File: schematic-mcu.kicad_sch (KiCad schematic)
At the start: 25 parts, among them U5 USBLC6-2P6, U6 ESP32-S3FN8, Y1 Crystal_GND24

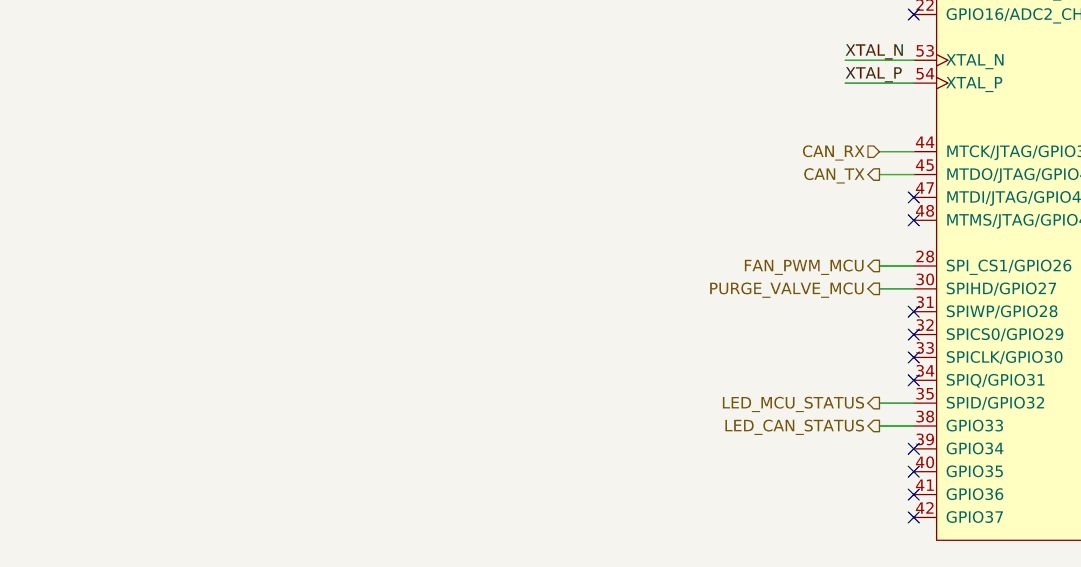
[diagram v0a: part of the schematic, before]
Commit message: Add power stages
Valve, power supplay, fan
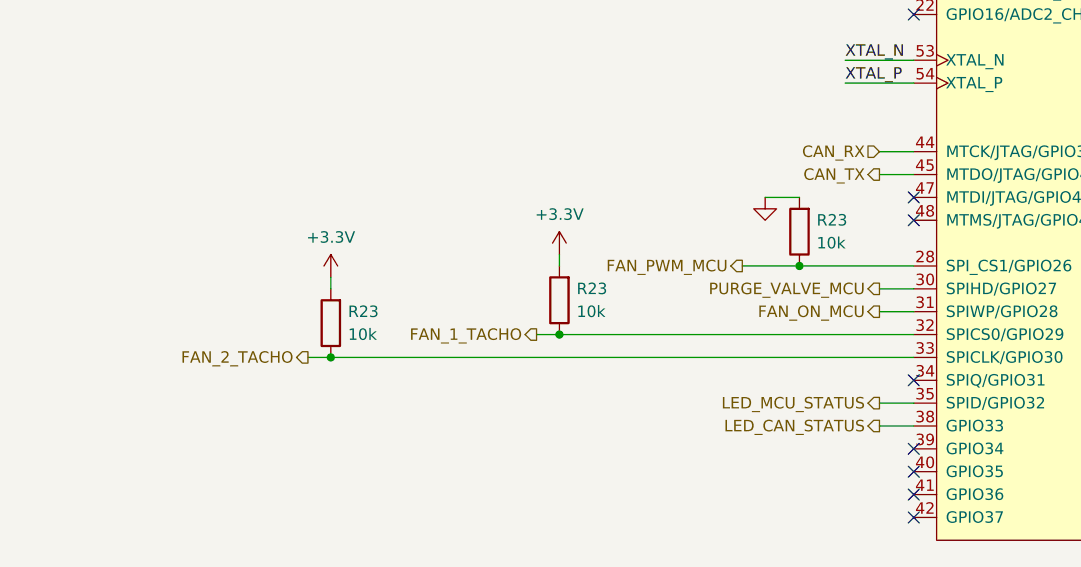
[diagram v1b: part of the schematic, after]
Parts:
- added R23 (x3): 10k, symbol Device:R
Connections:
- net +3.3V: now also R23.2, R23.2
- net FAN_PWM_MCU: now also R23.1
- net GND: now also R23.2
- net FAN_ON_MCU: now reaches U6.31 (SPIWP/GPIO28)
- net FAN_1_TACHO: now reaches U6.32 (SPICS0/GPIO29)
- net FAN_1_TACHO: now also R23.1
- net FAN_2_TACHO: now reaches U6.33 (SPICLK/GPIO30)
- net FAN_2_TACHO: now also R23.1
- no-connect marks 37 -> 34

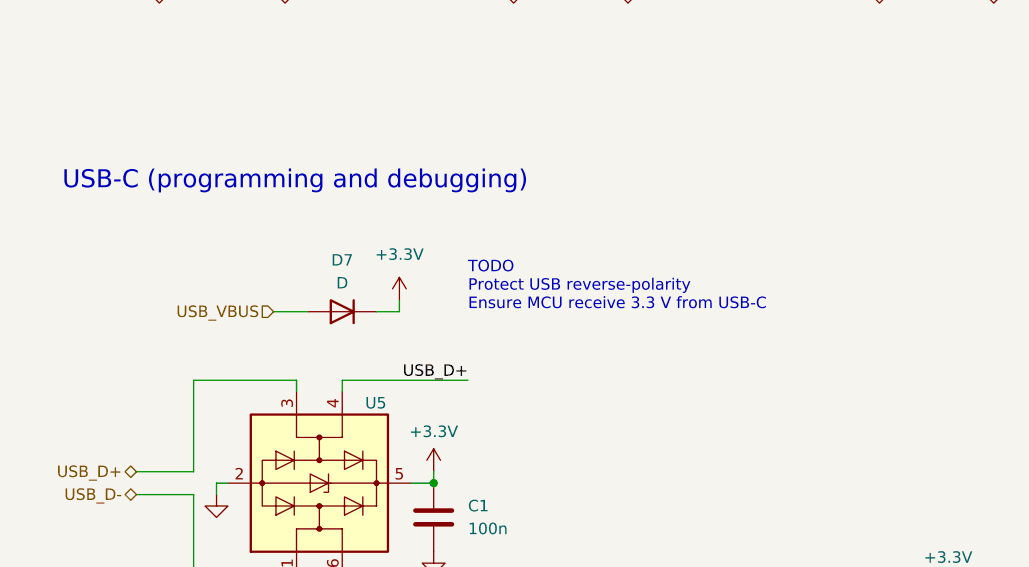
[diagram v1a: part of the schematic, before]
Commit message: Add Schottky Diode for VBUS and Vreg
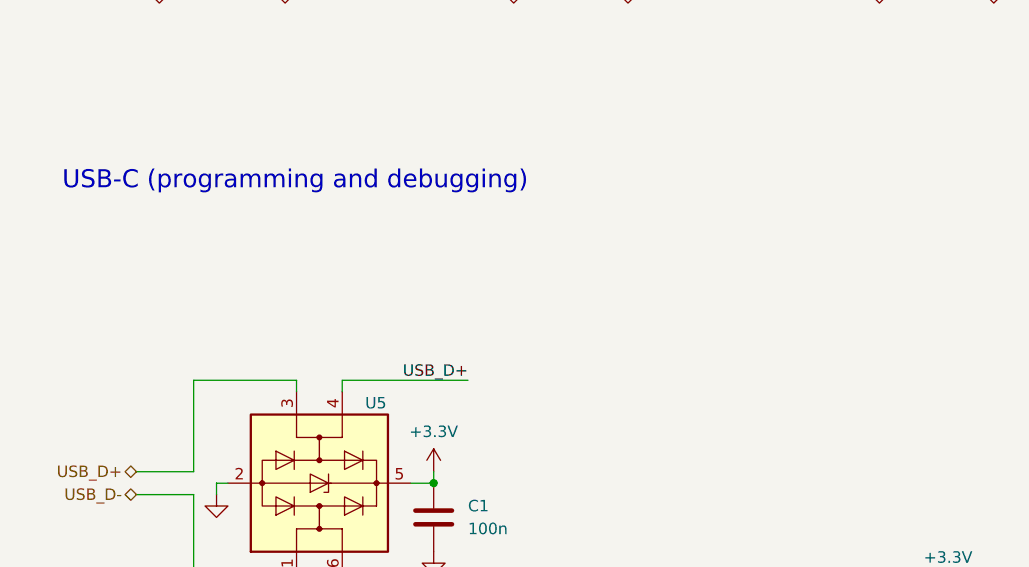
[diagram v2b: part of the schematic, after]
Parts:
- removed D7: D, symbol Device:D
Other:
- note removed: "TODO Protect USB reverse-polarity Ensure MCU receive 3.3 V from USB-C"
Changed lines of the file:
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@@
-    (stroke (width 0) (type default))
-  )
-  (wire (pts (xy 69.85 87.63) (xy 69.85 86.36))
     (stroke (width 0) (type default))
   )
@@
     (stroke (width 0) (type default))
   )
-  (wire (pts (xy 55.88 87.63) (xy 59.69 87.63))
-    (stroke (width 0) (type default))
-  )
   (wire (pts (xy 191.77 135.89) (xy 195.58 135.89))
     (stroke (width 0) (type default))
@@
   )
   (wire (pts (xy 270.51 85.09) (xy 261.62 85.09))
-    (stroke (width 0) (type default))
-  )
-  (wire (pts (xy 67.31 87.63) (xy 69.85 87.63))
     (stroke (width 0) (type default))
   )
@@
   (text "Microcontroller" (at 214.63 22.86 0)
     (effects (font (size 2 2)) (justify left bottom))
-  )
-  (text "TODO\nProtect USB reverse-polarity\nEnsure MCU receive 3.3 V from USB-C\n"
-    (at 77.47 87.63 0)
-    (effects (font (size 1.27 1.27)) (justify left bottom))
   )
   (text "Reset button" (at 49.53 25.4 0)
@@
   )
   (hierarchical_label "FAN_PWM_MCU" (shape output) (at 176.53 118.11 180) (fields_autoplaced)
-    (effects (font (size 1.27 1.27)) (justify right))
-  )
-  (hierarchical_label "USB_VBUS" (shape input) (at 55.88 87.63 180) (fields_autoplaced)
     (effects (font (size 1.27 1.27)) (justify right))
   )
@@
     )
   )
-  (symbol (lib_id "power:+3.3V") (at 69.85 86.36 0) (unit 1)
-    (in_bom yes) (on_board yes) (dnp no) (fields_autoplaced)
-    (property "Reference" "#PWR036" (at 69.85 90.17 0)
-      (effects (font (size 1.27 1.27)) hide)
-    )
-    (property "Value" "+3.3V" (at 69.85 81.28 0)
-      (effects (font (size 1.27 1.27)))
-    )
-    (property "Footprint" "" (at 69.85 86.36 0)
-      (effects (font (size 1.27 1.27)) hide)
-    )
-    (property "Datasheet" "" (at 69.85 86.36 0)
-      (effects (font (size 1.27 1.27)) hide)
-    )
-    (pin "1")
-    (instances
-      (project "schematic-main"
-        (path "/c9ad7189-d3b2-414a-9743-efd8e57cd755"
-          (reference "#PWR036") (unit 1)
-        )
-        (path "/c9ad7189-d3b2-414a-9743-efd8e57cd755/f92f58ec-64e0-437c-bc00-8ae46a3b3054"
-          (reference "#PWR028") (unit 1)
-        )
-      )
-    )
-  )
   (symbol (lib_id "power:GND") (at 73.66 114.3 0) (unit 1)
     (in_bom yes) (on_board yes) (dnp no) (fields_autoplaced)
@@
         )
       )
-    )
-  )
-  (symbol (lib_id "Device:D") (at 63.5 87.63 180) (unit 1)
-    (in_bom yes) (on_board yes) (dnp no) (fields_autoplaced)
-    (property "Reference" "D7" (at 63.5 81.915 0)
-      (effects (font (size 1.27 1.27)))
-    )
-    (property "Value" "D" (at 63.5 84.455 0)
-      (effects (font (size 1.27 1.27)))
-    )
-    (property "Footprint" "" (at 63.5 87.63 0)
-      (effects (font (size 1.27 1.27)) hide)
-    )
-    (property "Datasheet" "~" (at 63.5 87.63 0)
-      (effects (font (size 1.27 1.27)) hide)
-    )
-    (property "Sim.Device" "D" (at 63.5 87.63 0)
-      (effects (font (size 1.27 1.27)) hide)
-    )
-    (property "Sim.Pins" "1=K 2=A" (at 63.5 87.63 0)
-      (effects (font (size 1.27 1.27)) hide)
-    )
-    (pin "1")
-    (pin "2")
-    (instances
-      (project "schematic-main"
-        (path "/c9ad7189-d3b2-414a-9743-efd8e57cd755"
-          (reference "D7") (unit 1)
-        )
-        (path "/c9ad7189-d3b2-414a-9743-efd8e57cd755/f92f58ec-64e0-437c-bc00-8ae46a3b3054"
-          (reference "D2") (unit 1)
-        )
-      )

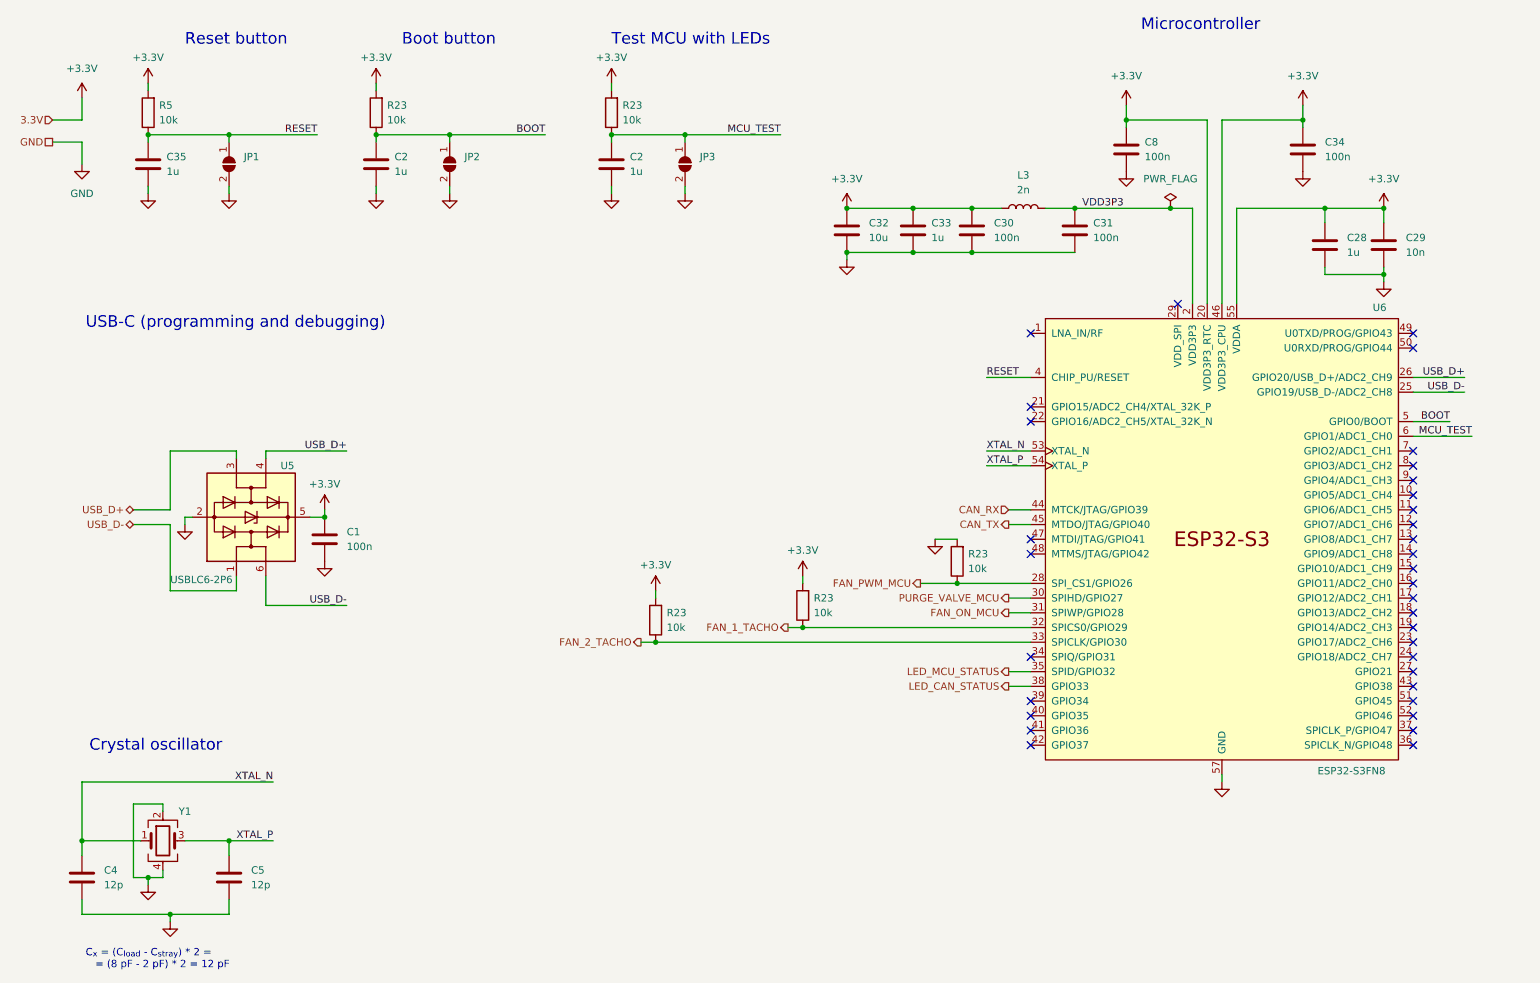
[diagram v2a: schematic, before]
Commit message: Add FC voltage measure, axilary input and output
Schematic complet?
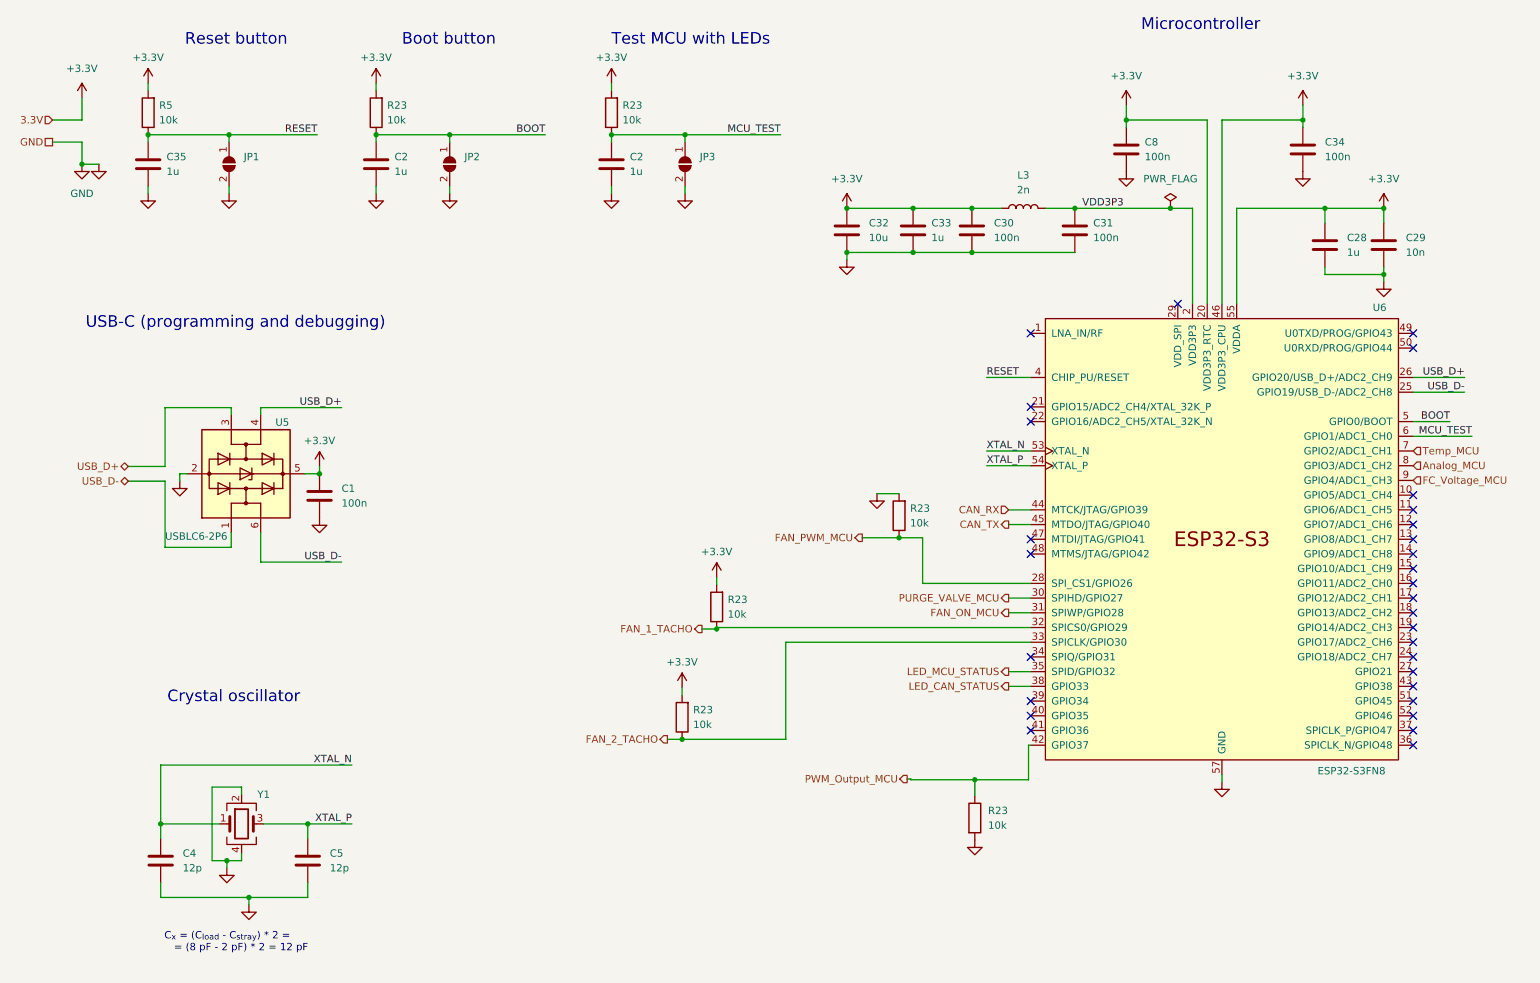
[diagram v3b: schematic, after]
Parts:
- added R23: 10k, symbol Device:R
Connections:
- net GND: now also R23.2
- net PWM_Output_MCU: now reaches U6.42 (GPIO37)
- net PWM_Output_MCU: now also R23.1
- net Temp_MCU: now reaches U6.7 (GPIO2/ADC1_CH1)
- net Analog_MCU: now reaches U6.8 (GPIO3/ADC1_CH2)
- net FC_Voltage_MCU: now reaches U6.9 (GPIO4/ADC1_CH3)
- no-connect marks 34 -> 30
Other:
- title: Motor driver unit -> Fuel Cell Control Unit  (FCCU)
- moved on the sheet: C1, C4, C5, R23, U5, Y1

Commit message: First pcb, change fan conector
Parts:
- C1, C2, C28, C29, C30, C31, C33, C34, C35, C4, C5, C8: footprint (none) -> Capacitor_SMD:C_1206_3216Metric
- C32: footprint (none) -> Capacitor_SMD:CP_Elec_8x10.5
- L3: footprint (none) -> Inductor_SMD:LQG15WH0N7B02D
- R23: footprint (none) -> LED_SMD:LED_1206_3216Metric
- R23, R5: footprint (none) -> Resistor_SMD:R_1206_3216Metric
- Y1: footprint (none) -> Crystal:KC3225K400000C1GE00
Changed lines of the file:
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@@
       (effects (font (size 1.27 1.27)) (justify left))
     )
-    (property "Footprint" "" (at 186.3852 60.96 0)
+    (property "Footprint" "Capacitor_SMD:C_1206_3216Metric" (at 186.3852 60.96 0)
       (effects (font (size 1.27 1.27)) hide)
     )
@@
       (effects (font (size 1.27 1.27)) (justify left))
     )
-    (property "Footprint" "" (at 164.7952 60.96 0)
+    (property "Footprint" "Capacitor_SMD:CP_Elec_8x10.5" (at 164.7952 60.96 0)
       (effects (font (size 1.27 1.27)) hide)
     )
@@
       (effects (font (size 1.27 1.27)) (justify left))
     )
-    (property "Footprint" "" (at 176.2252 60.96 0)
+    (property "Footprint" "Capacitor_SMD:C_1206_3216Metric" (at 176.2252 60.96 0)
       (effects (font (size 1.27 1.27)) hide)
     )
@@
       (effects (font (size 1.27 1.27)) (justify left))
     )
-    (property "Footprint" "" (at 213.0552 46.99 0)
+    (property "Footprint" "Capacitor_SMD:C_1206_3216Metric" (at 213.0552 46.99 0)
       (effects (font (size 1.27 1.27)) hide)
     )
@@
       (effects (font (size 1.27 1.27)) (justify left))
     )
-    (property "Footprint" "" (at 83.5152 49.53 0)
+    (property "Footprint" "Capacitor_SMD:C_1206_3216Metric" (at 83.5152 49.53 0)
       (effects (font (size 1.27 1.27)) hide)
     )
@@
       (effects (font (size 1.27 1.27)))
     )
-    (property "Footprint" "" (at 194.31 53.34 0)
+    (property "Footprint" "Inductor_SMD:LQG15WH0N7B02D" (at 194.31 53.34 0)
       (effects (font (size 1.27 1.27)) hide)
     )
@@
       (effects (font (size 1.27 1.27)) (justify left))
     )
-    (property "Footprint" "" (at 124.1552 49.53 0)
+    (property "Footprint" "Capacitor_SMD:C_1206_3216Metric" (at 124.1552 49.53 0)
       (effects (font (size 1.27 1.27)) hide)
     )
@@
       (effects (font (size 1.27 1.27)) (justify right))
     )
-    (property "Footprint" "" (at 124.968 36.83 90)
+    (property "Footprint" "LED_SMD:LED_1206_3216Metric" (at 124.968 36.83 90)
       (effects (font (size 1.27 1.27)) hide)
     )
@@
       (effects (font (size 1.27 1.27)) hide)
     )
-    (property "Footprint" "" (at 59.309 159.639 0)
+    (property "Footprint" "Crystal:KC3225K400000C1GE00" (at 59.309 159.639 0)
       (effects (font (size 1.27 1.27)) hide)
     )
@@
       (effects (font (size 1.27 1.27)) (justify left))
     )
-    (property "Footprint" "" (at 73.7362 106.807 0)
+    (property "Footprint" "Capacitor_SMD:C_1206_3216Metric" (at 73.7362 106.807 0)
       (effects (font (size 1.27 1.27)) hide)
     )
@@
       (effects (font (size 1.27 1.27)) (justify right))
     )
-    (property "Footprint" "" (at 44.958 36.83 90)
+    (property "Footprint" "Resistor_SMD:R_1206_3216Metric" (at 44.958 36.83 90)
       (effects (font (size 1.27 1.27)) hide)
     )
@@
       (effects (font (size 1.27 1.27)) (justify left))
     )
-    (property "Footprint" "" (at 257.5052 63.5 0)
+    (property "Footprint" "Capacitor_SMD:C_1206_3216Metric" (at 257.5052 63.5 0)
       (effects (font (size 1.27 1.27)) hide)
     )
@@
       (effects (font (size 1.27 1.27)) (justify left))
     )
-    (property "Footprint" "" (at 46.3042 169.799 0)
+    (property "Footprint" "Capacitor_SMD:C_1206_3216Metric" (at 46.3042 169.799 0)
       (effects (font (size 1.27 1.27)) hide)
     )
@@
       (effects (font (size 1.27 1.27)) (justify right))
     )
-    (property "Footprint" "" (at 174.625 106.426 90)
+    (property "Footprint" "LED_SMD:LED_1206_3216Metric" (at 174.625 106.426 90)
       (effects (font (size 1.27 1.27)) hide)
     )
@@
       (effects (font (size 1.27 1.27)) (justify right))
     )
-    (property "Footprint" "" (at 245.4148 63.5 0)
+    (property "Footprint" "Capacitor_SMD:C_1206_3216Metric" (at 245.4148 63.5 0)
       (effects (font (size 1.27 1.27)) hide)
     )
@@
       (effects (font (size 1.27 1.27)) (justify right))
     )
-    (property "Footprint" "" (at 84.328 36.83 90)
+    (property "Footprint" "Resistor_SMD:R_1206_3216Metric" (at 84.328 36.83 90)
       (effects (font (size 1.27 1.27)) hide)
     )
@@
       (effects (font (size 1.27 1.27)) (justify left))
     )
-    (property "Footprint" "" (at 243.5352 46.99 0)
+    (property "Footprint" "Capacitor_SMD:C_1206_3216Metric" (at 243.5352 46.99 0)
       (effects (font (size 1.27 1.27)) hide)
     )
@@
       (effects (font (size 1.27 1.27)) (justify left))
     )
-    (property "Footprint" "" (at 184.15 158.623 90)
+    (property "Footprint" "LED_SMD:LED_1206_3216Metric" (at 184.15 158.623 90)
       (effects (font (size 1.27 1.27)) hide)
     )
@@
       (effects (font (size 1.27 1.27)) (justify right))
     )
-    (property "Footprint" "" (at 143.129 122.174 90)
+    (property "Footprint" "LED_SMD:LED_1206_3216Metric" (at 143.129 122.174 90)
       (effects (font (size 1.27 1.27)) hide)
     )
@@
       (effects (font (size 1.27 1.27)) (justify right))
     )
-    (property "Footprint" "" (at 137.16 141.224 90)
+    (property "Footprint" "LED_SMD:LED_1206_3216Metric" (at 137.16 141.224 90)
       (effects (font (size 1.27 1.27)) hide)
     )
@@
       (effects (font (size 1.27 1.27)) (justify left))
     )
-    (property "Footprint" "" (at 204.1652 60.96 0)
+    (property "Footprint" "Capacitor_SMD:C_1206_3216Metric" (at 204.1652 60.96 0)
       (effects (font (size 1.27 1.27)) hide)
     )
@@
       (effects (font (size 1.27 1.27)) (justify left))
     )
-    (property "Footprint" "" (at 44.1452 49.53 0)
+    (property "Footprint" "Capacitor_SMD:C_1206_3216Metric" (at 44.1452 49.53 0)
       (effects (font (size 1.27 1.27)) hide)
     )
@@
       (effects (font (size 1.27 1.27)) (justify left))
     )
-    (property "Footprint" "" (at 71.7042 169.799 0)
-      (effects (font (size 1.27 1.27)) hide)
-    )
+    (property "Footprint" "Capacitor_SMD:C_1206_3216Metric" (at 71.7042 169.799 0)
+      (effects (font (size 1.27 1.27)) hide)
+    )
